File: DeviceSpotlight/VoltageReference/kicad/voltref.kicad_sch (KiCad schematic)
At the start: 14 parts, among them J1 IN, J2 LOWPASS OUT, J3 INTEGRATOR OUT, U1 TL072

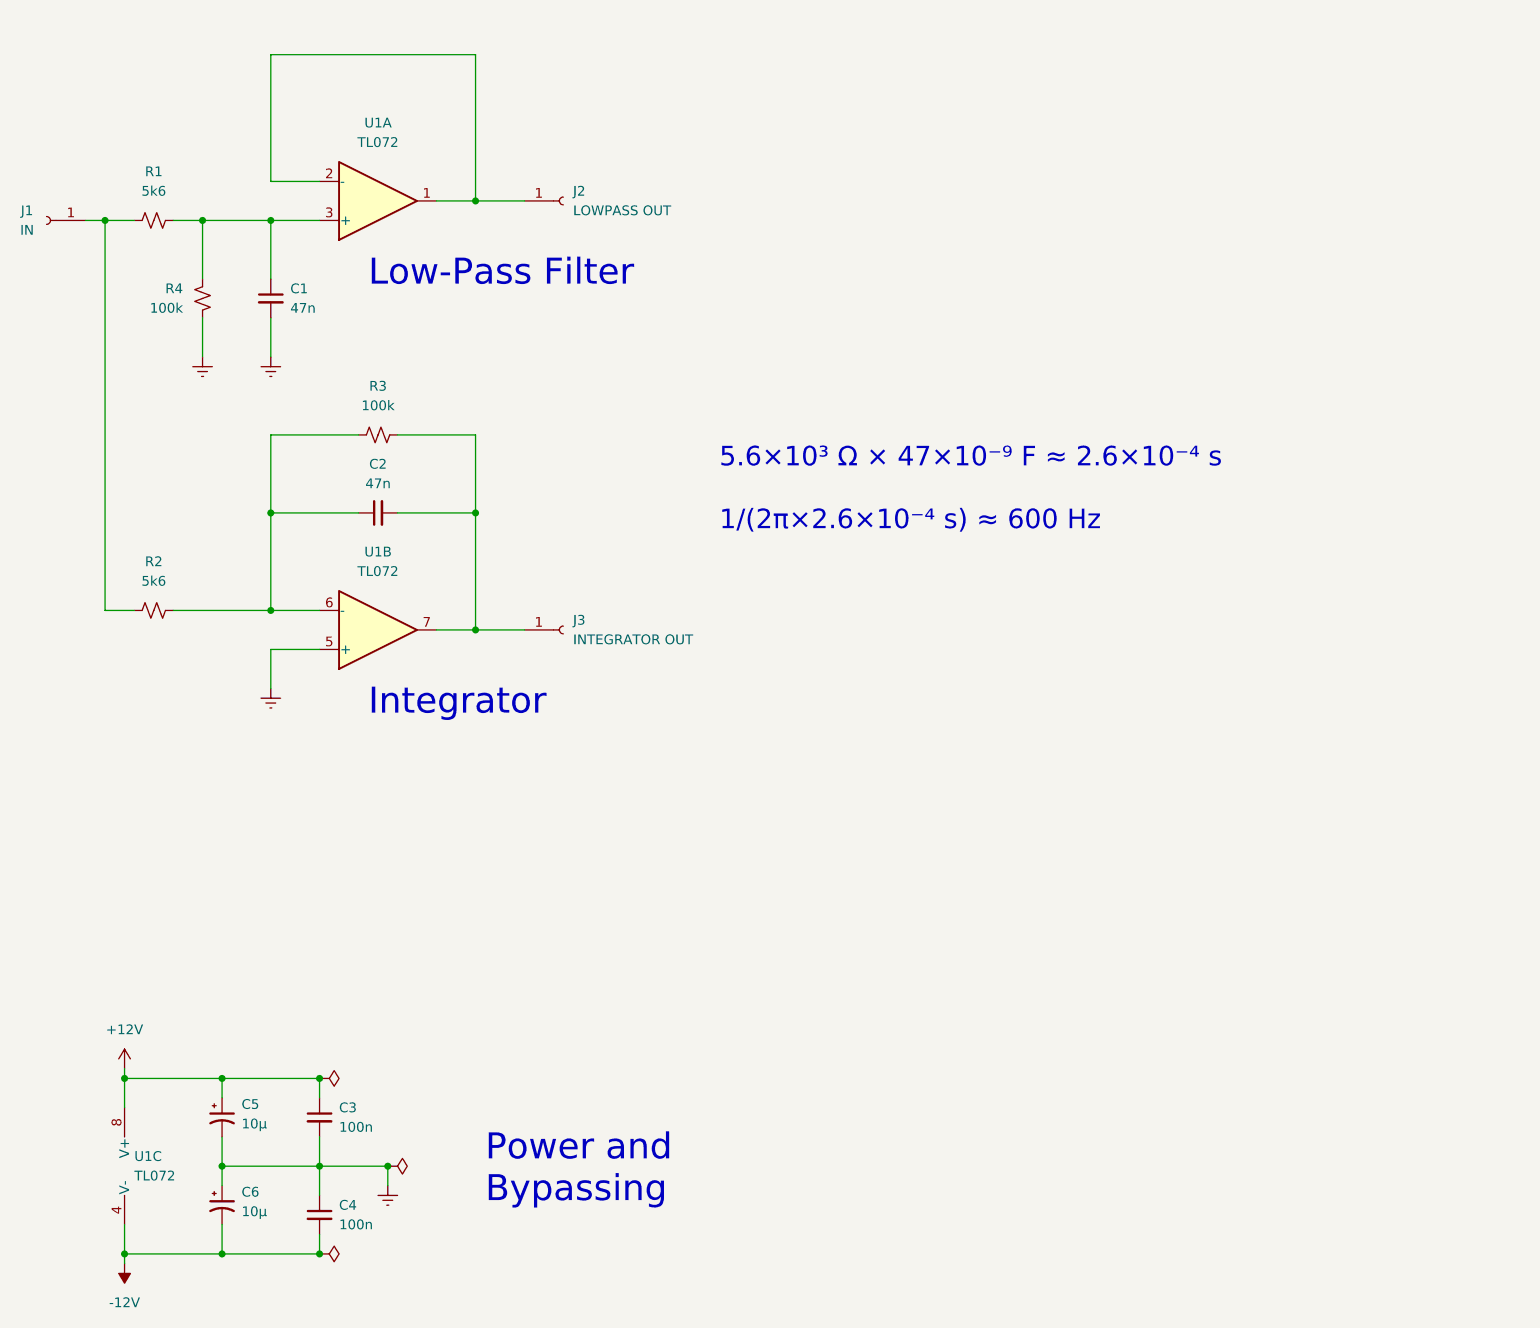
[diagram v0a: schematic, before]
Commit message: Updates to I-V tracer; add episode on TL431
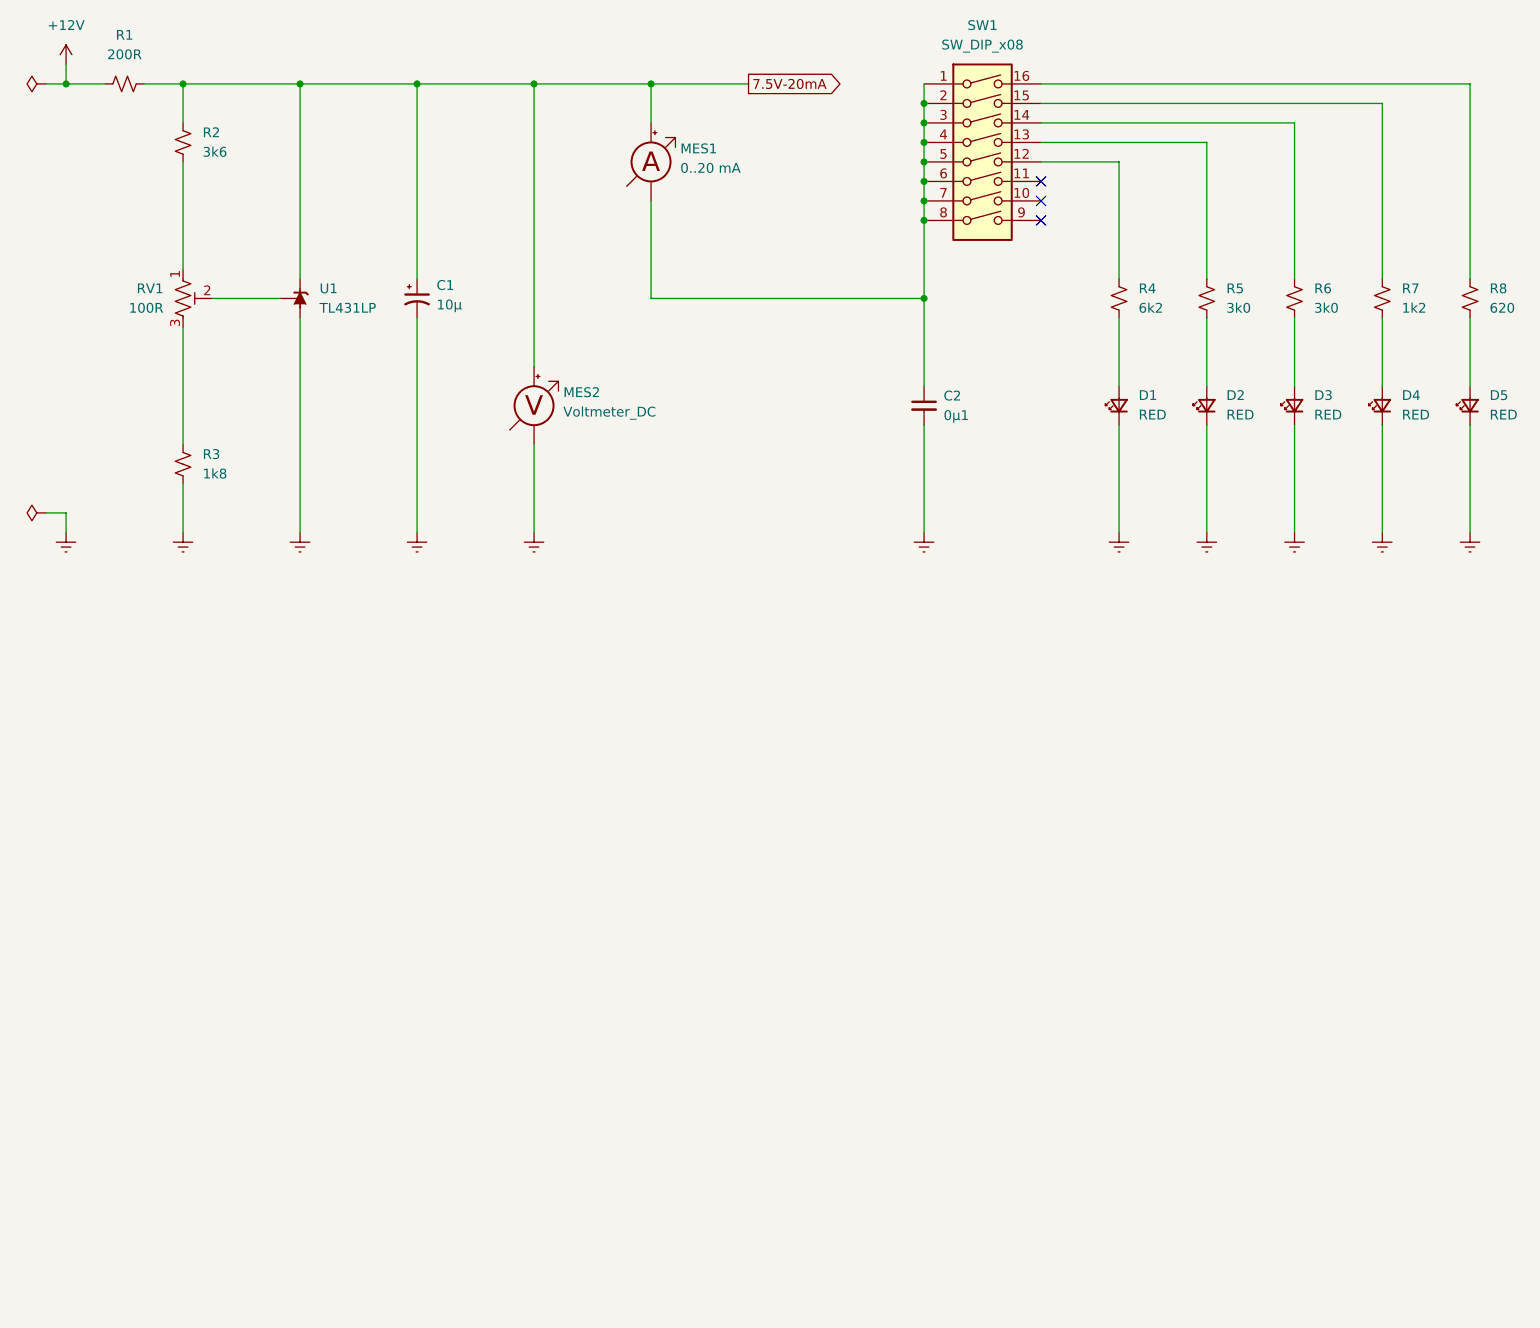
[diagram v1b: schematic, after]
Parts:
- removed C1: 47n, symbol Device:C_Small
- removed C3, C4: 100n, symbol Device:C_Small
- removed C5, C6: 10µ, symbol Device:C_Polarized_Small_US
- removed J1: IN, symbol Connector:Conn_01x01_Socket
- removed J2: LOWPASS OUT, symbol Connector:Conn_01x01_Socket
- removed J3: INTEGRATOR OUT, symbol Connector:Conn_01x01_Socket
- removed U1: TL072, symbol Amplifier_Operational:TL072
- added C1: 10µ, symbol Device:C_Polarized_Small_US
- added D1, D2, D3, D4, D5: RED, symbol Device:LED_Small
- added MES1: 0..20 mA, symbol Device:Ammeter_DC
- added MES2: Voltmeter_DC, symbol Device:Voltmeter_DC
- added R5, R6: 3k0, symbol Device:R_Small_US
- added R7: 1k2, symbol Device:R_Small_US
- added R8: 620, symbol Device:R_Small_US
- added RV1: 100R, symbol Device:R_Potentiometer_Trim_US
- added SW1: SW_DIP_x08, symbol Switch:SW_DIP_x08
- added U1: TL431LP, Package_TO_SOT_THT:TO-92_Inline, symbol Reference_Voltage:TL431LP
- C2: value 47n -> 0µ1
- R1: value 5k6 -> 200R
- R2: value 5k6 -> 3k6
- R3: value 100k -> 1k8
- R4: value 100k -> 6k2
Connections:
- net +12V: now also R1.1
- net Earth: now also C2.2, R3.1, C1.2, D1.1 (K), D2.1 (K), D3.1 (K), D4.1 (K), D5.1 (K), MES2.1 (-), U1.2 (A); no longer R4.1
- net at R3.2: now also RV1.3; no longer C2.2
- net at R2.1: now also RV1.1; no longer R1.1
- net at R4.2: now also SW1.12; no longer R1.2
- new net: C2.1, MES1.1 (-), SW1.1, SW1.2, SW1.3, SW1.4, SW1.5, SW1.6, SW1.7, SW1.8
- new net: D5.2 (A), R8.1
- new net: D4.2 (A), R7.1
- new net: D2.2 (A), R5.1
- new net: R7.2, SW1.15
- new net: D1.2 (A), R4.1
- new net: D3.2 (A), R6.1
- new net: R6.2, SW1.14
- new net: R5.2, SW1.13
- new net: R8.2, SW1.16
- new net: RV1.2, U1.1 (REF)
- new net 7.5V-20mA: C1.1, MES1.2 (+), MES2.2 (+), R1.2, R2.2, U1.3 (K)
- no-connect marks 0 -> 3
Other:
- note removed: "5.6×10³ Ω × 47×10⁻⁹ F ≈ 2.6×10⁻⁴ s 1/(2π×2.6×10⁻⁴ s) ≈ 600 Hz"
- note removed: "Integrator"
- note removed: "Low-Pass Filter"
- note removed: "Power and Bypassing"
- title: Low-Pass Filter vs. Integrator -> TL431 Demonstration Circuit
